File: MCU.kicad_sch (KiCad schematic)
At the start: 8 parts, among them J1 USB_C_Receptacle, U7 LSF0204GU12X, U8 FAN5622SX, X608 Display

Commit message: Updated MCU
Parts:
- added SW3, SW4, SW5, SW6: SW_Push, symbol Switch:SW_Push
- added U9: NORA-B106-00B, NORA-B106-00B:XCVR_NORA-B106-00B, symbol NORA-B106-00B:NORA-B106-00B
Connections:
- net 1V8: no longer C13.1, U7.1 (REFA)
- net DISPLAY_CLK: now also U9.B3 (P0.11/TRACEDATA0/CSN)
- net DISPLAY_CS: now also U9.A2 (P0.12/TRACECLK/DCX)
- net DISPLAY_DATA: now also U9.C1 (P0.10/TRACEDATA1/MISO)
- net DISPLAY_DC: now also U9.C2 (P0.09/TRACEDATA2/MOSI)
- net DISPLAY_LIGHT_IO: now also U9.G3 (P0.25/AIN4)
- net GND: now also SW3.1, SW4.1, SW5.1, SW6.1, U9.A1 (VSS), U9.A9 (VSS), U9.B2 (VSS), U9.B8 (VSS), U9.E4 (VSS), U9.E5 (VSS), U9.F4 (VSS), U9.F5 (VSS), U9.K2 (VSS), U9.K3 (VSS), U9.K5 (VSS), U9.K7 (VSS), U9.K8 (VSS), U9.L1 (VSS), U9.L9 (VSS), U9.M1 (VSS), U9.M2 (VSS), U9.M8 (VSS), U9.M9 (VSS)
- net TOUCH_EN: now also U9.D8 (P0.04/AIN0)
- net TOUCH_INT: now also U9.B1 (P0.08/TRACEDATA3/SCK)
- net TOUCH_RST: now also U9.E8 (P0.05/AIN1)
- net TOUCH_SCL: now also U9.D3 (P0.07/AIN3)
- net TOUCH_SDA: now also U9.E7 (P0.06/AIN2)
- net USBC_D+: now also U9.C9 (USB_DP)
- net USBC_D-: now also U9.D9 (USB_DM)
- net USB_RST: now reaches J1.A8 (SBU1)
- net USB_RST: now also J1.B8 (SBU2)
- new net: U9.A6 (NC), U9.J1 (NC), U9.J4 (NC), U9.J5 (NC), U9.K1 (NC), U9.K9 (NC)
- new net +1V8: C13.1, U7.1 (REFA), U9.A7 (VDD), U9.A8 (VDDH), U9.B7 (VDD)
- new net BMI_INT: U9.C8 (P0.22)
- new net BTN_1: SW4.2, U9.G2 (P0.26/AIN5)
- new net BTN_2: SW5.2, U9.B5 (P0.03/NFC2)
- new net BTN_3: SW6.2, U9.A4 (P1.00)
- new net LPS_INT: U9.A5 (P0.20)
- new net MAX_INT: U9.E3 (P0.21)
- new net MCU_RST: SW3.2, U9.J3 (~{RESET})
- new net OPT_INT: U9.D7 (P0.23)
- new net PMIC_INT: U9.H1 (P0.24)
- new net QSPI_CLK: U9.F1 (P0.17/SCK)
- new net QSPI_CS: U9.E1 (P0.18/CSN)
- new net QSPI_IO0: U9.D2 (P0.13/IO0)
- new net QSPI_IO1: U9.E2 (P0.14/IO1)
- new net QSPI_IO2: U9.D1 (P0.15/IO2)
- new net QSPI_IO3: U9.F2 (P0.16/IO3)
- new net SCL: U9.B4 (P1.02/TWI)
- new net SDA: U9.A3 (P1.03/TWI)
- new net SWCLK: U9.J2 (SWDCLK)
- new net SWDIO: U9.H2 (SWDIO)
- new net VBUS_OUT: U9.B9 (VBUS)
- no-connect marks 0 -> 14
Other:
- note added: "BUTTONS"
- note added: "MCU"
- note added: "NEED TO FIGURE OUT HOW TO PROGRAM"
- note added: "USBC"

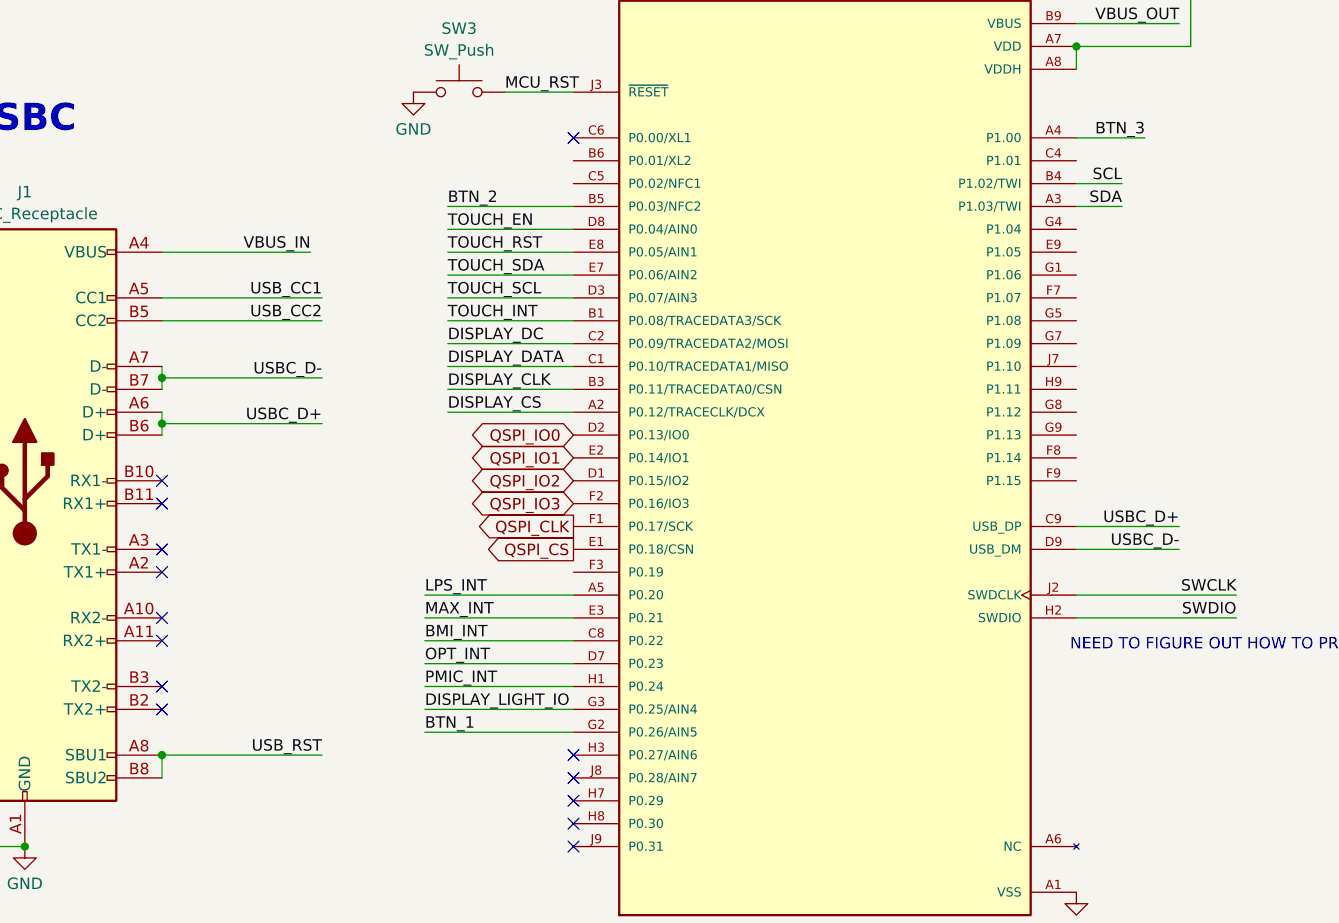
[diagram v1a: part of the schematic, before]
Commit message: Fixed Hierarchical Labels
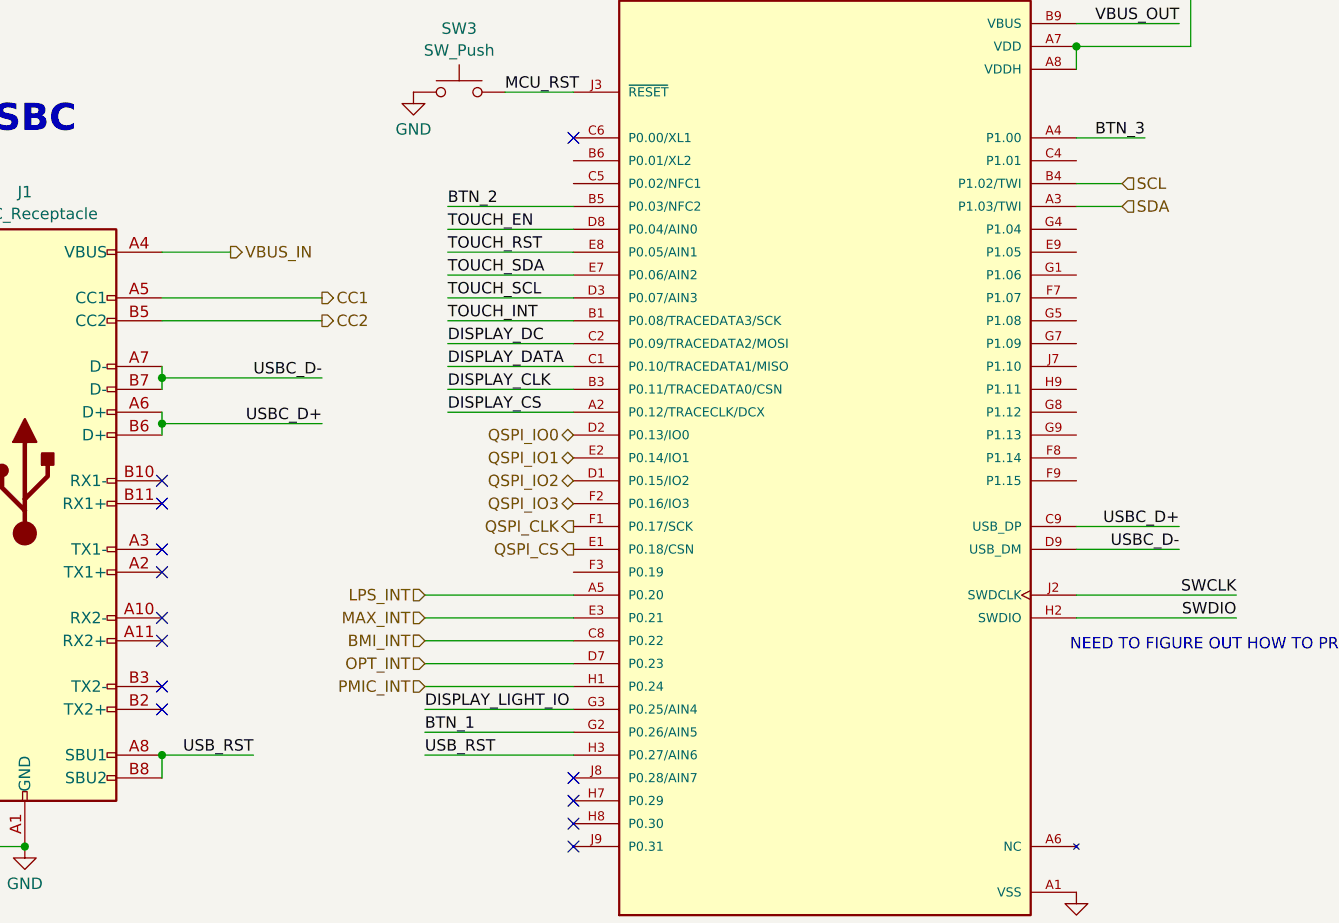
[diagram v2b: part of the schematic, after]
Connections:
- net USB_RST: now also U9.H3 (P0.27/AIN6)
- net USB_CC1 renamed CC1
- net USB_CC2 renamed CC2
- no-connect marks 14 -> 13
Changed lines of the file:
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@@
-	)
-	(no_connect
-		(at 99.06 124.46)
 	)
 	(no_connect
@@
 	(wire
 		(pts
-			(xy 53.34 124.46) (xy 71.12 124.46)
+			(xy 53.34 124.46) (xy 63.5 124.46)
 		)
 		(stroke
@@
 	(wire
 		(pts
-			(xy 53.34 68.58) (xy 69.85 68.58)
+			(xy 53.34 68.58) (xy 60.96 68.58)
 		)
 		(stroke
@@
 		(pts
 			(xy 166.37 43.18) (xy 154.94 43.18)
+		)
+		(stroke
+			(width 0)
+			(type default)
+		)
+	)
+	(wire
+		(pts
+			(xy 82.55 124.46) (xy 99.06 124.46)
 		)
 		(stroke
@@
 		)
 	)
-	(label "VBUS_IN"
-		(at 69.85 68.58 180)
-		(effects
-			(font
-				(size 1.27 1.27)
-			)
-			(justify right bottom)
-		)
-	)
 	(label "USBC_D+"
 		(at 71.12 87.63 180)
@@
 		)
 	)
-	(label "SDA"
-		(at 160.02 63.5 180)
-		(effects
-			(font
-				(size 1.27 1.27)
-			)
-			(justify right bottom)
-		)
-	)
 	(label "CTP_SDA"
 		(at 269.24 38.1 180)
@@
 		)
 	)
-	(label "BMI_INT"
-		(at 82.55 111.76 0)
-		(effects
-			(font
-				(size 1.27 1.27)
-			)
-			(justify left bottom)
-		)
-	)
 	(label "DISPLAY_RST"
 		(at 214.63 80.01 0)
@@
 		)
 	)
-	(label "LPS_INT"
-		(at 82.55 106.68 0)
-		(effects
-			(font
-				(size 1.27 1.27)
-			)
-			(justify left bottom)
-		)
-	)
 	(label "LEDK2"
 		(at 213.36 86.36 0)
@@
 		)
 	)
-	(label "OPT_INT"
-		(at 82.55 114.3 0)
-		(effects
-			(font
-				(size 1.27 1.27)
-			)
-			(justify left bottom)
-		)
-	)
 	(label "SWDIO"
 		(at 172.72 109.22 180)
@@
 	)
 	(label "USB_RST"
-		(at 71.12 124.46 180)
-		(effects
-			(font
-				(size 1.27 1.27)
-			)
-			(justify right bottom)
-		)
-	)
-	(label "MAX_INT"
-		(at 82.55 109.22 0)
-		(effects
-			(font
-				(size 1.27 1.27)
-			)
-			(justify left bottom)
-		)
-	)
-	(label "PMIC_INT"
-		(at 82.55 116.84 0)
-		(effects
-			(font
-				(size 1.27 1.27)
-			)
-			(justify left bottom)
+		(at 63.5 124.46 180)
+		(effects
+			(font
+				(size 1.27 1.27)
+			)
+			(justify right bottom)
 		)
 	)
@@
 		)
 	)
-	(label "USB_CC1"
-		(at 71.12 73.66 180)
-		(effects
-			(font
-				(size 1.27 1.27)
-			)
-			(justify right bottom)
-		)
-	)
 	(label "DISPLAY_DC"
 		(at 85.09 78.74 0)
@@
 		)
 	)
-	(label "SCL"
-		(at 160.02 60.96 180)
-		(effects
-			(font
-				(size 1.27 1.27)
-			)
-			(justify right bottom)
-		)
-	)
 	(label "DISPLAY_LIGHT_IO"
 		(at 82.55 119.38 0)
@@
 		)
 	)
-	(label "USB_CC2"
-		(at 71.12 76.2 180)
-		(effects
-			(font
-				(size 1.27 1.27)
-			)
-			(justify right bottom)
-		)
-	)
 	(label "TOUCH_SCL"
 		(at 85.09 73.66 0)
@@
 		)
 	)
+	(label "USB_RST"
+		(at 82.55 124.46 0)
+		(effects
+			(font
+				(size 1.27 1.27)
+			)
+			(justify left bottom)
+		)
+	)
 	(label "BTN_2"
 		(at 57.15 171.45 180)
@@
 		)
 	)
-	(global_label "QSPI_IO0"
+	(hierarchical_label "SCL"
+		(shape input)
+		(at 160.02 60.96 0)
+		(effects
+			(font
+				(size 1.27 1.27)
+			)
+			(justify left)
+		)
+	)
+	(hierarchical_label "LPS_INT"
+		(shape input)
+		(at 82.55 106.68 180)
+		(effects
+			(font
+				(size 1.27 1.27)
+			)
+			(justify right)
+		)
+	)
+	(hierarchical_label "QSPI_CLK"
+		(shape output)
+		(at 99.06 99.06 180)
+		(effects
+			(font
+				(size 1.27 1.27)
+			)
+			(justify right)
+		)
+	)
+	(hierarchical_label "QSPI_IO2"
+		(shape bidirectional)
+		(at 99.06 93.98 180)
+		(effects
+			(font
+				(size 1.27 1.27)
+			)
+			(justify right)
+		)
+	)
+	(hierarchical_label "CC2"
+		(shape output)
+		(at 71.12 76.2 0)
+		(effects
+			(font
+				(size 1.27 1.27)
+			)
+			(justify left)
+		)
+	)
+	(hierarchical_label "CC1"
+		(shape output)
+		(at 71.12 73.66 0)
+		(effects
+			(font
+				(size 1.27 1.27)
+			)
+			(justify left)
+		)
+	)
+	(hierarchical_label "QSPI_IO1"
+		(shape bidirectional)
+		(at 99.06 91.44 180)
+		(effects
+			(font
+				(size 1.27 1.27)
+			)
+			(justify right)
+		)
+	)
+	(hierarchical_label "PMIC_INT"
+		(shape input)
+		(at 82.55 116.84 180)
+		(effects
+			(font
+				(size 1.27 1.27)
+			)
+			(justify right)
+		)
+	)
+	(hierarchical_label "QSPI_CS"
+		(shape output)
+		(at 99.06 101.6 180)
+		(effects
+			(font
+				(size 1.27 1.27)
+			)
+			(justify right)
+		)
+	)
+	(hierarchical_label "SDA"
+		(shape input)
+		(at 160.02 63.5 0)
+		(effects
+			(font
+				(size 1.27 1.27)
+			)
+			(justify left)
+		)
+	)
+	(hierarchical_label "OPT_INT"
+		(shape input)
+		(at 82.55 114.3 180)
+		(effects
+			(font
+				(size 1.27 1.27)
+			)
+			(justify right)
+		)
+	)
+	(hierarchical_label "BMI_INT"
+		(shape input)
+		(at 82.55 111.76 180)
+		(effects
+			(font
+				(size 1.27 1.27)
+			)
+			(justify right)
+		)
+	)
+	(hierarchical_label "QSPI_IO3"
+		(shape bidirectional)
+		(at 99.06 96.52 180)
+		(effects
+			(font
+				(size 1.27 1.27)
+			)
+			(justify right)
+		)
+	)
+	(hierarchical_label "QSPI_IO0"
 		(shape bidirectional)
 		(at 99.06 88.9 180)
-		(fields_autoplaced yes)
 		(effects
 			(font
@@
 			(justify right)
 		)
-		(property "Intersheetrefs" "${INTERSHEET_REFS}"
-			(at 86.4363 88.9 0)
-			(effects
-				(font
-					(size 1.27 1.27)
-				)
-				(justify right)
-				(hide yes)
-			)
-		)
-	)
-	(global_label "QSPI_IO1"
-		(shape bidirectional)
-		(at 99.06 91.44 180)
-		(fields_autoplaced yes)
+	)
+	(hierarchical_label "MAX_INT"
+		(shape input)
+		(at 82.55 109.22 180)
 		(effects
 			(font
@@
 			(justify right)
 		)
-		(property "Intersheetrefs" "${INTERSHEET_REFS}"
-			(at 86.4363 91.44 0)
-			(effects
-				(font
-					(size 1.27 1.27)
-				)
-				(justify right)
-				(hide yes)
-			)
-		)
-	)
-	(global_label "QSPI_CLK"
+	)
+	(hierarchical_label "VBUS_IN"
 		(shape output)
-		(at 99.06 99.06 180)
-		(fields_autoplaced yes)
-		(effects
-			(font
-				(size 1.27 1.27)
-			)
-			(justify right)
-		)
-		(property "Intersheetrefs" "${INTERSHEET_REFS}"
-			(at 87.1243 99.06 0)
-			(effects
-				(font
-					(size 1.27 1.27)
-				)
-				(justify right)
-				(hide yes)
-			)
-		)
-	)
-	(global_label "QSPI_CS"
-		(shape output)
-		(at 99.06 101.6 180)
-		(fields_autoplaced yes)
-		(effects
-			(font
-				(size 1.27 1.27)
-			)
-			(justify right)
-		)
-		(property "Intersheetrefs" "${INTERSHEET_REFS}"
-			(at 88.2129 101.6 0)
-			(effects
-				(font
-					(size 1.27 1.27)
-				)
-				(justify right)
-				(hide yes)
-			)
-		)
-	)
-	(global_label "QSPI_IO3"
-		(shape bidirectional)
-		(at 99.06 96.52 180)
-		(fields_autoplaced yes)
-		(effects
-			(font
-				(size 1.27 1.27)
-			)
-			(justify right)
-		)
-		(property "Intersheetrefs" "${INTERSHEET_REFS}"
-			(at 86.4363 96.52 0)
-			(effects
-				(font
-					(size 1.27 1.27)
-				)
-				(justify right)
-				(hide yes)
-			)
-		)
-	)
-	(global_label "QSPI_IO2"
-		(shape bidirectional)
-		(at 99.06 93.98 180)
-		(fields_autoplaced yes)
-		(effects
-			(font
-				(size 1.27 1.27)
-			)
-			(justify right)
-		)
-		(property "Intersheetrefs" "${INTERSHEET_REFS}"
-			(at 86.4363 93.98 0)
-			(effects
-				(font
-					(size 1.27 1.27)
-				)
-				(justify right)
-				(hide yes)
-			)
-		)
-	)
+		(at 60.96 68.58 0)
+		(effects
+			(font
+				(size 1.27 1.27)
+			)
+			(justify left)
+		)
+	)
